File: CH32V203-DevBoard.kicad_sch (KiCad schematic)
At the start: 41 parts, among them J1 USB_C_Receptacle_USB2.0_16P, J2 USB_C_Receptacle_USB2.0_16P, Q1 AO3401A, Q2 AO3401A, SW1 SW_Push, SW2 SW_Push, U1 CH32V203C8T6, U2 RT9080-33GJ5

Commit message: USB周りの配線や裏面シルクの修正
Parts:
- U2: JLCPCB Rotation Offset -90 -> 90
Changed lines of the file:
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@@
 			)
 		)
-		(property "JLCPCB Rotation Offset" "-90"
+		(property "JLCPCB Rotation Offset" "90"
 			(at 115.57 60.96 0)
 			(effects

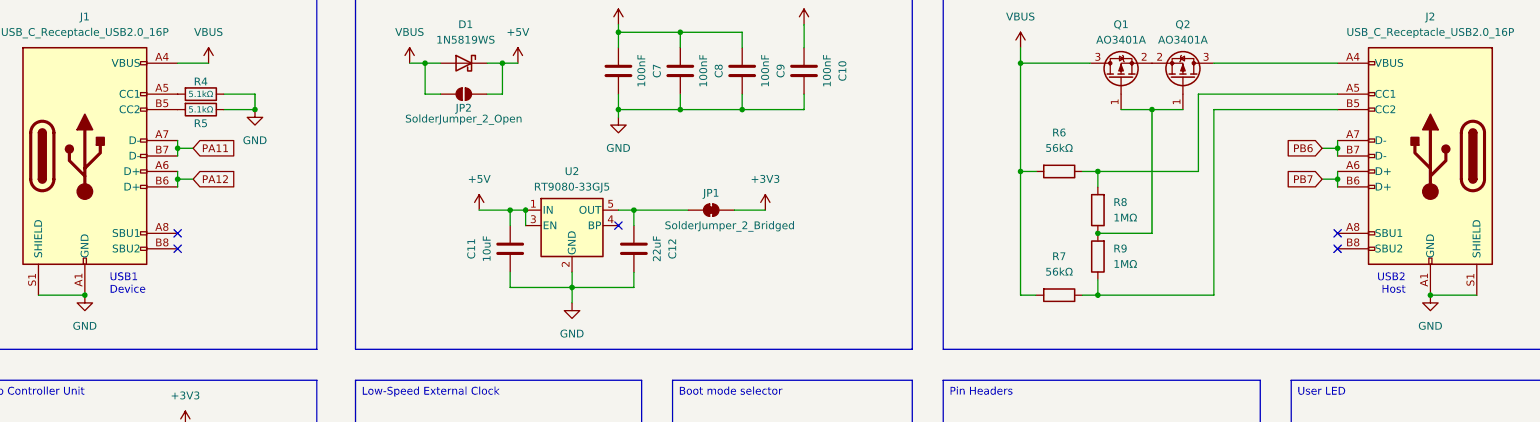
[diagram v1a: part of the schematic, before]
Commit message: add usb2 device solder jumper
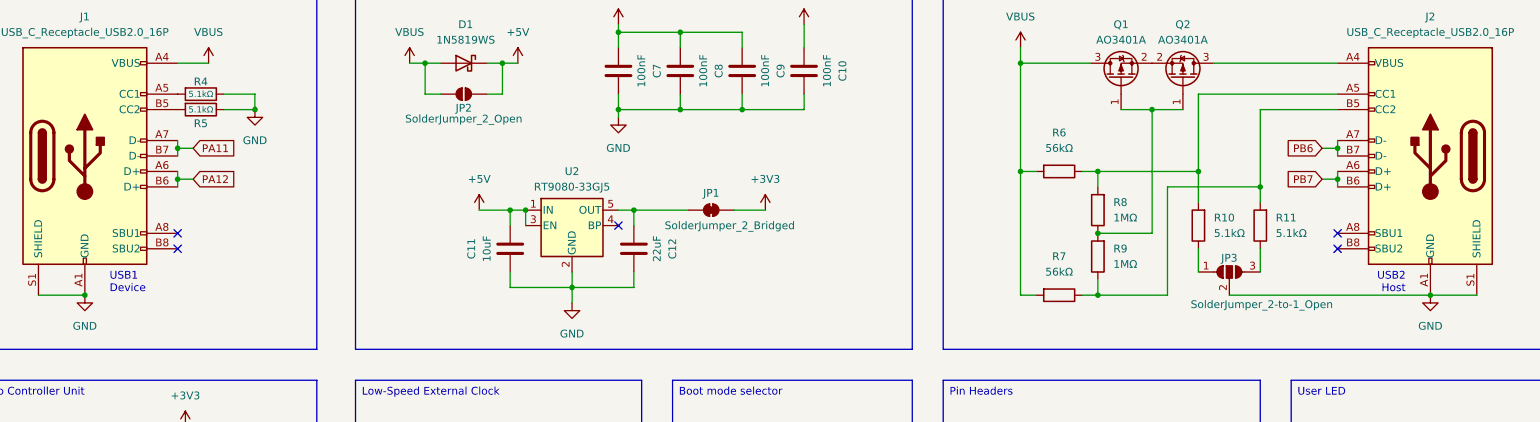
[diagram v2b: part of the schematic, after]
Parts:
- added JP3: SolderJumper_2-to-1_Open, SolderJumper:SolderJumper-2-to-1_P0.9mm_Open, symbol Jumper:SolderJumper_3_Open
- added R10, R11: 5.1kΩ, Resistor_SMD:R_0402_1005Metric, symbol Device:R
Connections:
- net GND: now also JP3.2 (C)
- net at J2.B5 (CC2), R7.1, R9.1: now also R11.2
- net at J2.A5 (CC1), R6.1, R8.2: now also R10.2
- new net: JP3.1 (A), R10.1
- new net: JP3.3 (B), R11.1

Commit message: fix JLCPCB Offset
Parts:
- J1, J2: JLCPCB Position Offset 0, 1.27 -> (none)
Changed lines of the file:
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@@
-			)
-		)
-		(property "JLCPCB Position Offset" "0, 1.27"
-			(at 256.54 49.53 0)
-			(effects
-				(font
-					(size 1.27 1.27)
-				)
-				(hide yes)
 			)
 		)
@@
 			(at 35.56 49.53 0)
 			(effects
-				(font
-					(size 1.27 1.27)
-				)
-				(hide yes)
-			)
-		)
-		(property "JLCPCB Position Offset" "0, 1.27"
-			(at 35.56 49.53 0)
-			(effects

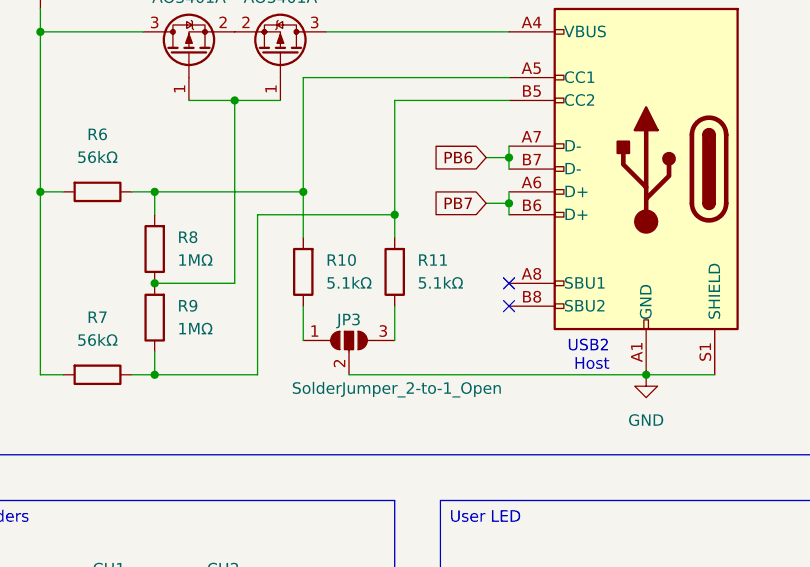
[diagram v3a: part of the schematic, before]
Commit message: pulldown resistor fix
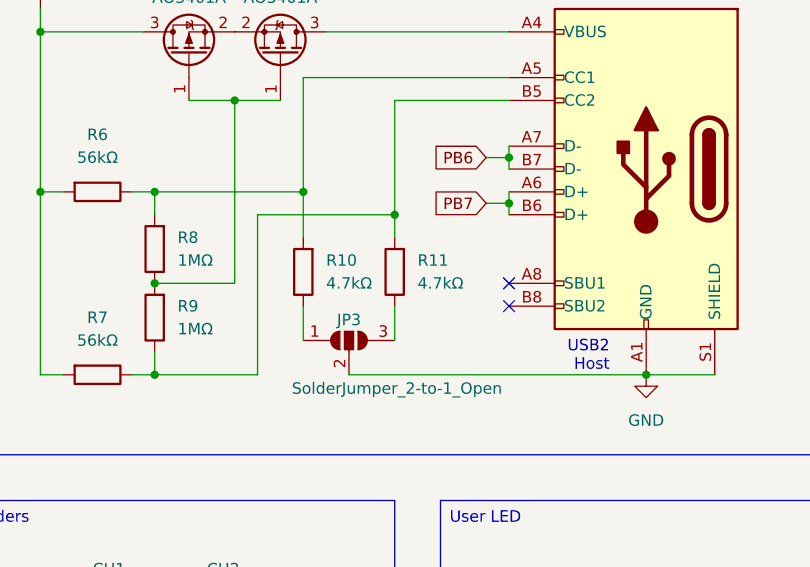
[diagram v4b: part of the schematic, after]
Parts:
- R10, R11: value 5.1kΩ -> 4.7kΩ; LCSC C25905 -> C25900
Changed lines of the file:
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@@
 			)
 		)
-		(property "Value" "5.1kΩ"
+		(property "Value" "4.7kΩ"
 			(at 220.98 62.2299 0)
 			(effects
@@
 			)
 		)
-		(property "LCSC" "C25905"
+		(property "LCSC" "C25900"
 			(at 218.44 60.96 90)
 			(effects
@@
 			)
 		)
-		(property "Value" "5.1kΩ"
+		(property "Value" "4.7kΩ"
 			(at 231.14 62.2299 0)
 			(effects
@@
 			)
 		)
-		(property "LCSC" "C25905"
+		(property "LCSC" "C25900"
 			(at 228.6 60.96 90)
 			(effects

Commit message: remove unused property
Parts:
- XTAL1, XTAL2: JLCPCB Rotation Offset 0 -> (none)
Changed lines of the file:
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@@
-			)
-		)
-		(property "JLCPCB Rotation Offset" "0"
-			(at 105.41 105.41 90)
-			(effects
-				(font
-					(size 1.27 1.27)
-				)
-				(hide yes)
 			)
 		)
@@
 			(at 106.68 143.51 90)
 			(effects
-				(font
-					(size 1.27 1.27)
-				)
-				(hide yes)
-			)
-		)
-		(property "JLCPCB Rotation Offset" "0"
-			(at 106.68 143.51 90)
-			(effects

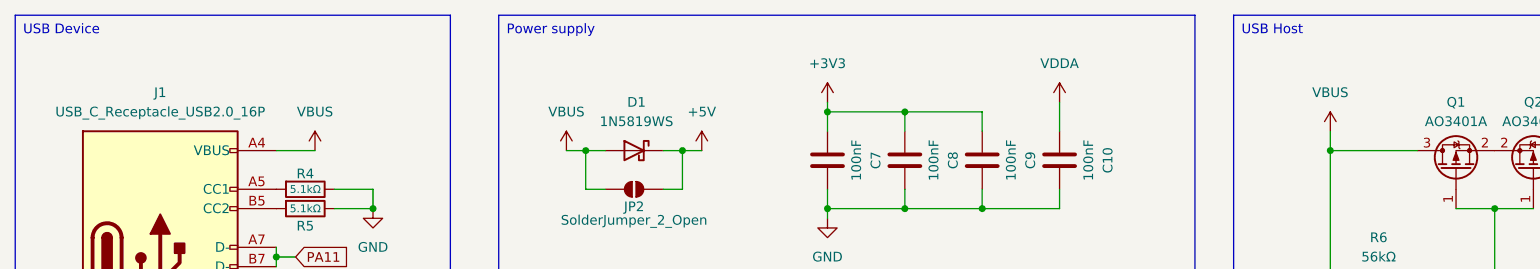
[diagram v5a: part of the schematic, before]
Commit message: fix wire width
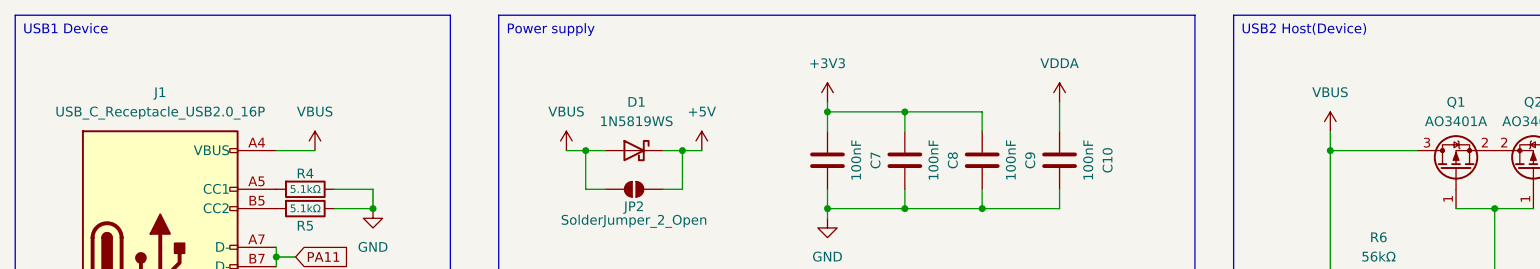
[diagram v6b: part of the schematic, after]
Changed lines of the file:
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@@
 		)
 	)
-	(text_box "USB Device"
+	(text_box "USB1 Device"
 		(exclude_from_sim no)
 		(at 16.51 16.51 0)
@@
 		)
 	)
-	(text_box "USB Host"
+	(text_box "USB2 Host(Device)"
 		(exclude_from_sim no)
 		(at 176.53 16.51 0)

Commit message: fix default usb position
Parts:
- J1, J2: JLCPCB Position Offset (none) -> 0, 0.127
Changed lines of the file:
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@@
+			)
+		)
+		(property "JLCPCB Position Offset" "0, 0.127"
+			(at 256.54 49.53 0)
+			(effects
+				(font
+					(size 1.27 1.27)
+				)
+				(hide yes)
 			)
 		)
@@
 			(at 35.56 49.53 0)
 			(effects
+				(font
+					(size 1.27 1.27)
+				)
+				(hide yes)
+			)
+		)
+		(property "JLCPCB Position Offset" "0, 0.127"
+			(at 35.56 49.53 0)
+			(effects

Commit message: change usb component
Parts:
- J1, J2: JLCPCB Position Offset 0, 0.127 -> 0, 0.13; LCSC C2765186 -> C2988369
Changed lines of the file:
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@@
 			)
 		)
-		(property "LCSC" "C2765186"
+		(property "LCSC" "C2988369"
 			(at 256.54 49.53 0)
 			(effects
@@
 			)
 		)
-		(property "JLCPCB Position Offset" "0, 0.127"
+		(property "JLCPCB Position Offset" "0, 0.13"
 			(at 256.54 49.53 0)
 			(effects
@@
 			)
 		)
-		(property "LCSC" "C2765186"
+		(property "LCSC" "C2988369"
 			(at 35.56 49.53 0)
 			(effects
@@
 			)
 		)
-		(property "JLCPCB Position Offset" "0, 0.127"
+		(property "JLCPCB Position Offset" "0, 0.13"
 			(at 35.56 49.53 0)
 			(effects
